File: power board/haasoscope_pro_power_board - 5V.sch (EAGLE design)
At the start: 147 parts, among them CN1 12Vin, IC11 TPS7A7200RGTR, IC12 TPS7A7200RGTR, IC14 TPS7A7200RGTR, IC3 TPS7A7200RGTR, IC5 TPS72325DBVR, IC7 TPS7A7200RGTR, IC9 TPS7A7200RGTR, J1 2p-2.54, J10 2p-2.54, J11 2p-2.54, J12 2p-2.54, J13 2p-2.54, J14 2p-2.54, J15 2p-2.54, J16 8pin, J17 2p-2.54, J18 2p-2.54, J19 2p-2.54, J2 2p-2.54, J20 2p-2.54, J3 2p-2.54, J4 2p-2.54, J5 2p-2.54, J6 2p-2.54, J7 2p-2.54, J8 2p-2.54, J9 2p-2.54

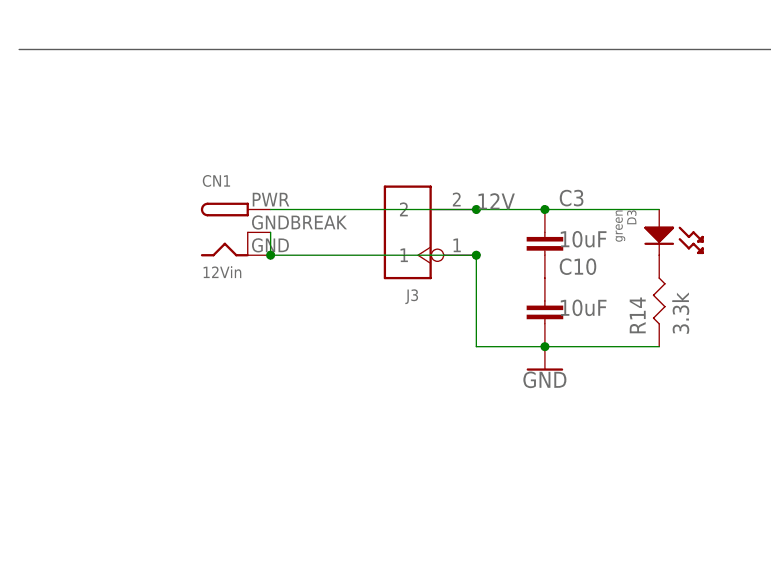
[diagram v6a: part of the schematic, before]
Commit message: add another 12V 10uF cap
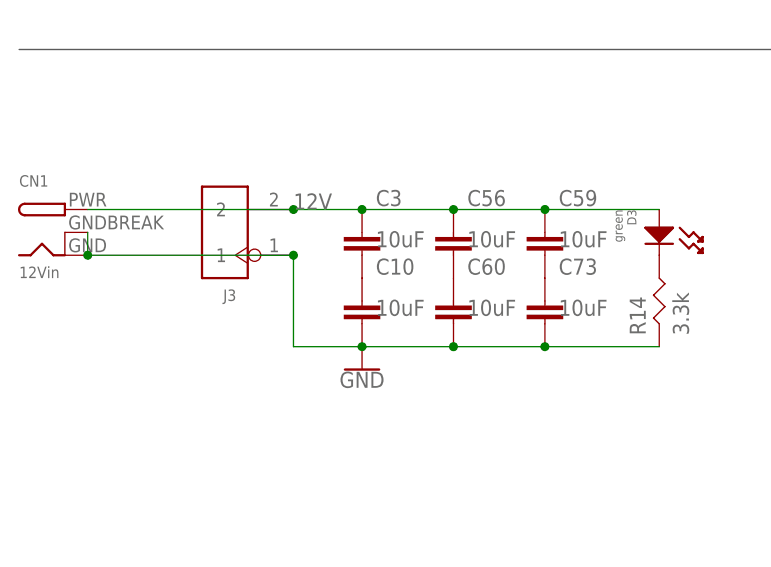
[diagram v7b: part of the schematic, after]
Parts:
- added C56, C59, C60, C73: 10uF, Nordic_nRF:CAPACITOR_0805_N
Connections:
- new net N$15: C56.2, C60.1
- new net N$40: C59.2, C73.1
- net 12V: now also C56.1, C59.1
- net GND: now also C60.2, C73.2
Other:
- moved on the sheet: C10, C3, CN1, J3
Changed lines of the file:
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@@
 <attribute name="LCSC" value="C307331"/>
 </part>
+<part name="C56" library="Nordic_nRF" library_urn="urn:adsk.eagle:library:169009" deviceset="CAPACITOR" device="_0805_N" package3d_urn="urn:adsk.eagle:package:2593736/1" value="10uF"/>
+<part name="C59" library="Nordic_nRF" library_urn="urn:adsk.eagle:library:169009" deviceset="CAPACITOR" device="_0805_N" package3d_urn="urn:adsk.eagle:package:2593736/1" value="10uF"/>
+<part name="C60" library="Nordic_nRF" library_urn="urn:adsk.eagle:library:169009" deviceset="CAPACITOR" device="_0805_N" package3d_urn="urn:adsk.eagle:package:2593736/1" value="10uF"/>
+<part name="C73" library="Nordic_nRF" library_urn="urn:adsk.eagle:library:169009" deviceset="CAPACITOR" device="_0805_N" package3d_urn="urn:adsk.eagle:package:2593736/1" value="10uF"/>
 </parts>
 <sheets>
@@
 </plain>
 <instances>
-<instance part="GND1" gate="1" x="58.42" y="-101.6" smashed="yes">
-<attribute name="VALUE" x="58.42" y="-101.854" size="1.778" layer="96" align="top-center"/>
-</instance>
-<instance part="J3" gate="G$1" x="43.18" y="-86.36" smashed="yes" rot="R180">
-<attribute name="NAME" x="44.45" y="-92.71" size="1.27" layer="95" ratio="10" rot="R180"/>
-</instance>
-<instance part="C3" gate="C$1" x="58.42" y="-86.36" smashed="yes">
-<attribute name="NAME" x="59.944" y="-83.439" size="1.778" layer="95"/>
-<attribute name="VALUE" x="59.944" y="-88.011" size="1.778" layer="96"/>
-</instance>
-<instance part="C10" gate="C$1" x="58.42" y="-93.98" smashed="yes">
-<attribute name="NAME" x="59.944" y="-91.059" size="1.778" layer="95"/>
-<attribute name="VALUE" x="59.944" y="-95.631" size="1.778" layer="96"/>
+<instance part="GND1" gate="1" x="38.1" y="-101.6" smashed="yes">
+<attribute name="VALUE" x="38.1" y="-101.854" size="1.778" layer="96" align="top-center"/>
+</instance>
+<instance part="J3" gate="G$1" x="22.86" y="-86.36" smashed="yes" rot="R180">
+<attribute name="NAME" x="24.13" y="-92.71" size="1.27" layer="95" ratio="10" rot="R180"/>
+</instance>
+<instance part="C3" gate="C$1" x="38.1" y="-86.36" smashed="yes">
+<attribute name="NAME" x="39.624" y="-83.439" size="1.778" layer="95"/>
+<attribute name="VALUE" x="39.624" y="-88.011" size="1.778" layer="96"/>
+</instance>
+<instance part="C10" gate="C$1" x="38.1" y="-93.98" smashed="yes">
+<attribute name="NAME" x="39.624" y="-91.059" size="1.778" layer="95"/>
+<attribute name="VALUE" x="39.624" y="-95.631" size="1.778" layer="96"/>
 </instance>
 <instance part="IC3" gate="G$1" x="246.38" y="317.5" smashed="yes">
@@
 </instance>
 <instance part="J16" gate="G$1" x="35.56" y="-134.62" smashed="yes" rot="R180"/>
-<instance part="CN1" gate="G$1" x="25.4" y="-86.36" smashed="yes">
-<attribute name="NAME" x="20.32" y="-81.28" size="1.27" layer="95"/>
-<attribute name="VALUE" x="20.32" y="-91.44" size="1.27" layer="96"/>
+<instance part="CN1" gate="G$1" x="5.08" y="-86.36" smashed="yes">
+<attribute name="NAME" x="0" y="-81.28" size="1.27" layer="95"/>
+<attribute name="VALUE" x="0" y="-91.44" size="1.27" layer="96"/>
 </instance>
 <instance part="J17" gate="G$1" x="238.76" y="160.02" smashed="yes" rot="R180">
@@
 <attribute name="VALUE" x="98.044" y="-100.711" size="1.778" layer="96"/>
 <attribute name="LCSC" x="96.52" y="-96.52" size="1.778" layer="96" display="off"/>
+</instance>
+<instance part="C56" gate="C$1" x="48.26" y="-86.36" smashed="yes">
+<attribute name="NAME" x="49.784" y="-83.439" size="1.778" layer="95"/>
+<attribute name="VALUE" x="49.784" y="-88.011" size="1.778" layer="96"/>
+</instance>
+<instance part="C59" gate="C$1" x="58.42" y="-86.36" smashed="yes">
+<attribute name="NAME" x="59.944" y="-83.439" size="1.778" layer="95"/>
+<attribute name="VALUE" x="59.944" y="-88.011" size="1.778" layer="96"/>
+</instance>
+<instance part="C60" gate="C$1" x="48.26" y="-93.98" smashed="yes">
+<attribute name="NAME" x="49.784" y="-91.059" size="1.778" layer="95"/>
+<attribute name="VALUE" x="49.784" y="-95.631" size="1.778" layer="96"/>
+</instance>
+<instance part="C73" gate="C$1" x="58.42" y="-93.98" smashed="yes">
+<attribute name="NAME" x="59.944" y="-91.059" size="1.778" layer="95"/>
+<attribute name="VALUE" x="59.944" y="-95.631" size="1.778" layer="96"/>
 </instance>
 </instances>
@@
 <segment>
 <pinref part="J3" gate="G$1" pin="1"/>
-<wire x1="50.8" y1="-88.9" x2="50.8" y2="-99.06" width="0.1524" layer="91"/>
+<wire x1="30.48" y1="-88.9" x2="30.48" y2="-99.06" width="0.1524" layer="91"/>
 <pinref part="GND1" gate="1" pin="GND"/>
 <pinref part="C10" gate="C$1" pin="2"/>
-<junction x="58.42" y="-99.06"/>
-<wire x1="58.42" y1="-99.06" x2="50.8" y2="-99.06" width="0.1524" layer="91"/>
+<junction x="38.1" y="-99.06"/>
+<wire x1="38.1" y1="-99.06" x2="30.48" y2="-99.06" width="0.1524" layer="91"/>
 <pinref part="R14" gate="G$1" pin="P$1"/>
 <wire x1="71.12" y1="-99.06" x2="58.42" y2="-99.06" width="0.1524" layer="91"/>
 <pinref part="CN1" gate="G$1" pin="GND"/>
-<wire x1="27.94" y1="-88.9" x2="50.8" y2="-88.9" width="0.1524" layer="91"/>
-<junction x="50.8" y="-88.9"/>
+<wire x1="58.42" y1="-99.06" x2="48.26" y2="-99.06" width="0.1524" layer="91"/>
+<wire x1="48.26" y1="-99.06" x2="38.1" y2="-99.06" width="0.1524" layer="91"/>
+<wire x1="7.62" y1="-88.9" x2="30.48" y2="-88.9" width="0.1524" layer="91"/>
+<junction x="30.48" y="-88.9"/>
 <pinref part="CN1" gate="G$1" pin="GNDBREAK"/>
-<wire x1="27.94" y1="-86.36" x2="27.94" y2="-88.9" width="0.1524" layer="91"/>
-<junction x="27.94" y="-88.9"/>
+<wire x1="7.62" y1="-86.36" x2="7.62" y2="-88.9" width="0.1524" layer="91"/>
+<junction x="7.62" y="-88.9"/>
+<pinref part="C60" gate="C$1" pin="2"/>
+<junction x="48.26" y="-99.06"/>
+<pinref part="C73" gate="C$1" pin="2"/>
+<junction x="58.42" y="-99.06"/>
 </segment>
 <segment>
@@
 </segment>
 <segment>
-<wire x1="50.8" y1="-83.82" x2="58.42" y2="-83.82" width="0.1524" layer="91"/>
-<label x="50.8" y="-83.82" size="1.778" layer="95"/>
+<wire x1="30.48" y1="-83.82" x2="38.1" y2="-83.82" width="0.1524" layer="91"/>
+<label x="30.48" y="-83.82" size="1.778" layer="95"/>
 <pinref part="J3" gate="G$1" pin="2"/>
 <pinref part="C3" gate="C$1" pin="1"/>
 <pinref part="D3" gate="G$1" pin="ANODE"/>
 <wire x1="71.12" y1="-83.82" x2="58.42" y2="-83.82" width="0.1524" layer="91"/>
+<junction x="38.1" y="-83.82"/>
+<pinref part="CN1" gate="G$1" pin="PWR"/>
+<wire x1="58.42" y1="-83.82" x2="48.26" y2="-83.82" width="0.1524" layer="91"/>
+<wire x1="48.26" y1="-83.82" x2="38.1" y2="-83.82" width="0.1524" layer="91"/>
+<wire x1="30.48" y1="-83.82" x2="7.62" y2="-83.82" width="0.1524" layer="91"/>
+<junction x="30.48" y="-83.82"/>
+<pinref part="C56" gate="C$1" pin="1"/>
+<junction x="48.26" y="-83.82"/>
+<pinref part="C59" gate="C$1" pin="1"/>
 <junction x="58.42" y="-83.82"/>
-<pinref part="CN1" gate="G$1" pin="PWR"/>
-<wire x1="50.8" y1="-83.82" x2="27.94" y2="-83.82" width="0.1524" layer="91"/>
-<junction x="50.8" y="-83.82"/>
 </segment>
 </net>
@@
 </segment>
 </net>
+<net name="N$15" class="0">
+<segment>
+<pinref part="C56" gate="C$1" pin="2"/>
+<pinref part="C60" gate="C$1" pin="1"/>
+</segment>
+</net>
+<net name="N$40" class="0">
+<segment>
+<pinref part="C59" gate="C$1" pin="2"/>
+<pinref part="C73" gate="C$1" pin="1"/>
+</segment>
+</net>

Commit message: 2.4->2.2V for 1.9V reg, to reduce heat add vias in regulator gnd pads, to dissipate heat
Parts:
- removed J17, J18, J19: 2p-2.54, Seeed-Connector:DIP-BLACK-MALE-HEADER-VERT(2P-2.54)
- R6: value 100k -> 82k
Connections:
- net 2V4 renamed 2V2
- removed net N$10: IC7.100MV, J17.2
- removed net N$8: IC3.100MV, J19.2
- removed net N$9: IC9.100MV, J18.2
- net GND: no longer J17.1, J18.1, J19.1
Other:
- note added: "12V input, in case USB C insufficient"
- note added: "5V input, needed unless there is 12V input"
- note added: "Outputs"
- note added: "Rbot = Rtop/(Vout-1) =82k/(2.2-1) = ~68k"
- note added: "V for 1.9V reg ~ 2.2V"
- note removed: "Rbot = Rtop/(Vout-1) =100k/(2.4-1) = ~71k"
- note removed: "V for 1.9V reg ~ 2.4V"
- moved on the sheet: C1, C2, D1, J1, R1
